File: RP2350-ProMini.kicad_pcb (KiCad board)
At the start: 4 copper layers, 17.8 x 41.9 mm, 46 parts, among them J1 CONN_L, J2 CONN_U, J3 CONN_R2, J4 CONN_R, J5 CONN_R3, J6 USB_B_Micro, J7 CONN_JTAG, Q1 AO3400A, U1 W25Q128JVS, U2 RP2350A-QFN60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

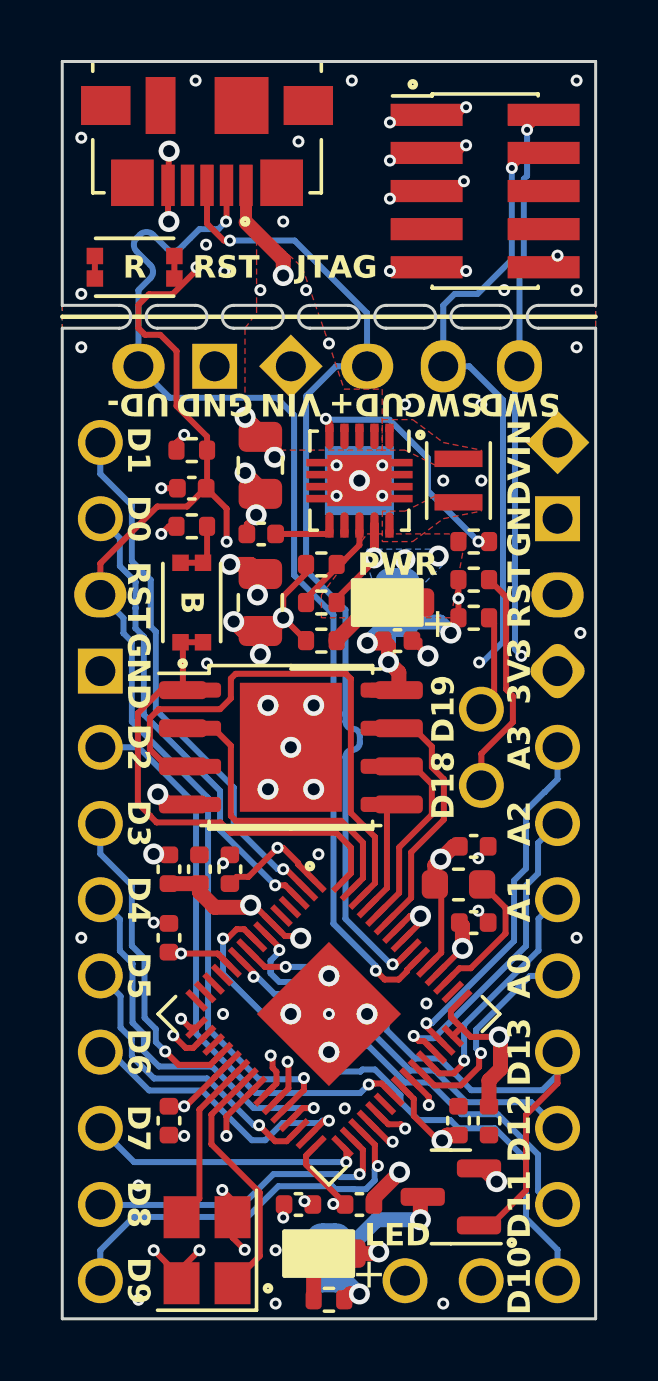
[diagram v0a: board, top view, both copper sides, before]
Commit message: Moved staff around.
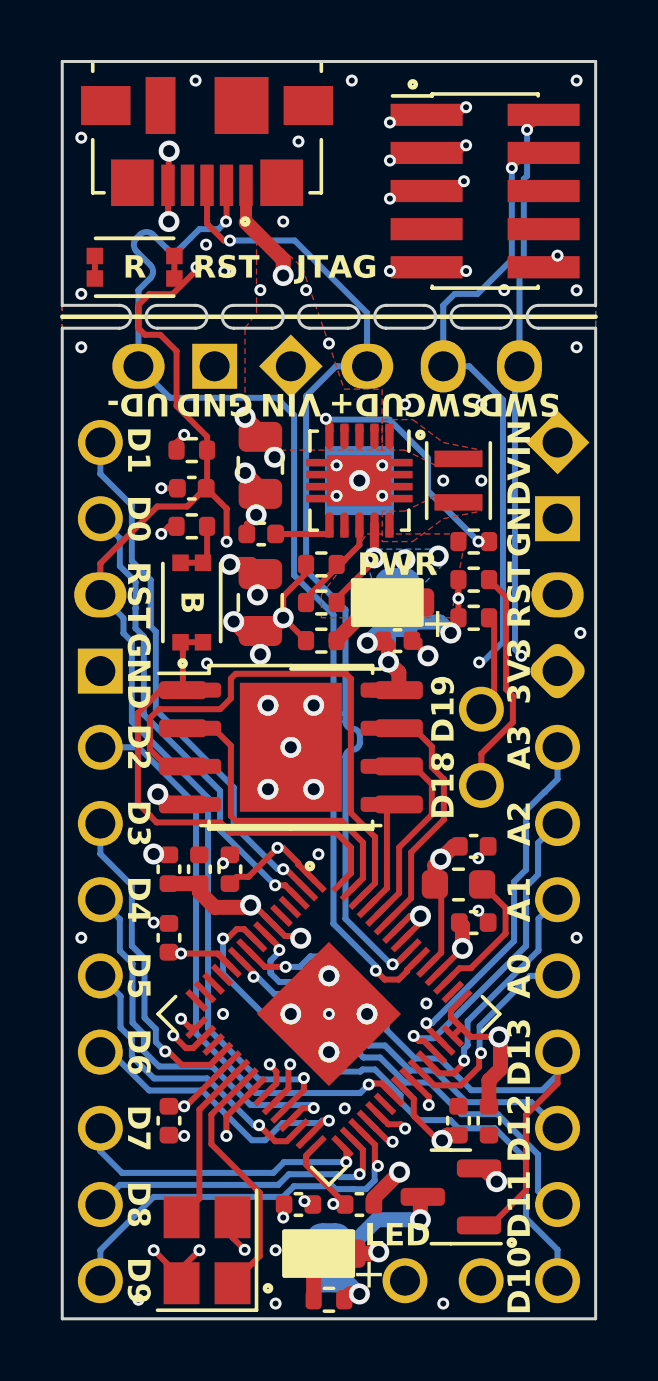
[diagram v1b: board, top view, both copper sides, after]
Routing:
- net GND: track 30.4 -> 29.4 mm, vias 76 -> 74
- net D7: track 9.24 -> 9.99 mm
- net SWD: track 38.9 -> 38.4 mm
